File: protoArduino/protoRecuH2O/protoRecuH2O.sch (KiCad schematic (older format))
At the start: 1 part

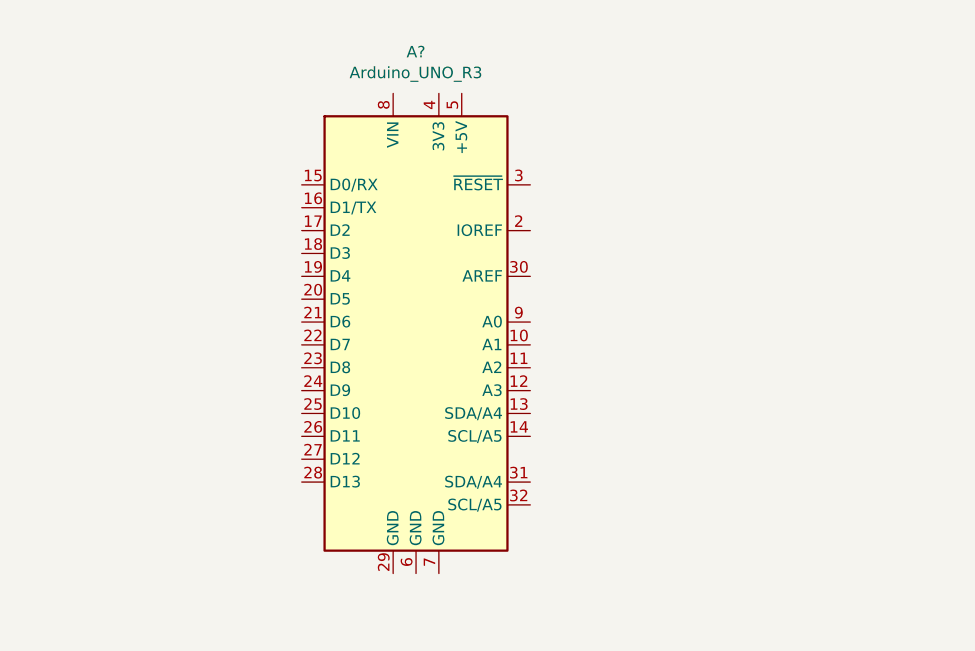
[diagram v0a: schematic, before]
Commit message: schéma éléctrique
j'ai ajouté la arduino, le graph bar, les résistances et le servo moteur avec tout le câblage. Il me reste plus que le câblage de la sonde à faire
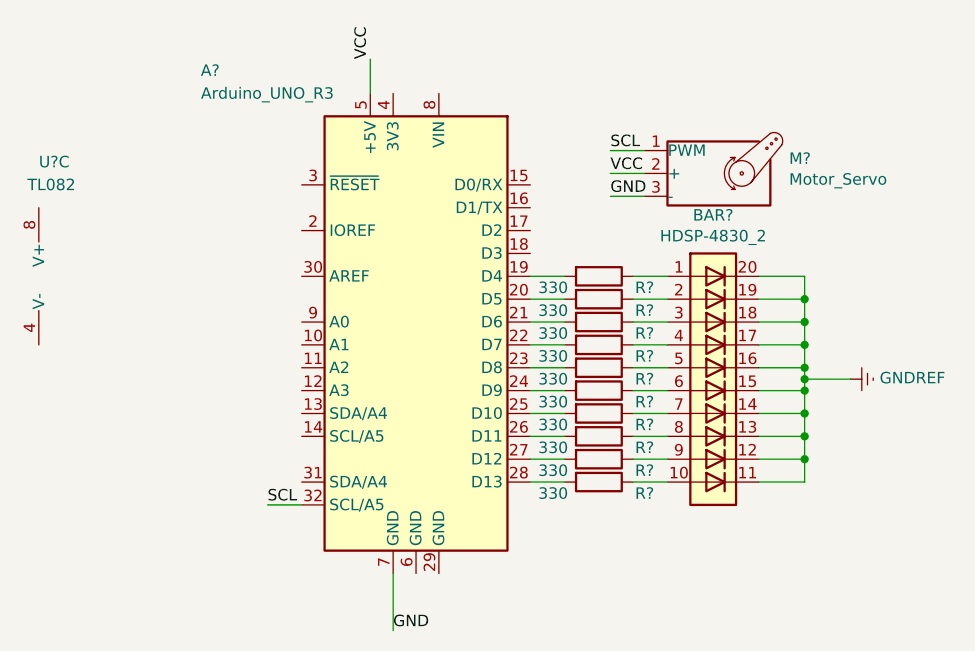
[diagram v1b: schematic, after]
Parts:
- added BAR?: HDSP-4830_2, Display:HDSP-4830, symbol LED:HDSP-4830_2
- added M?: Motor_Servo, symbol Motor:Motor_Servo
- added R? (x10): 330, symbol Device:R
- added U?: TL082, symbol Amplifier_Operational:TL082
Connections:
- net at A?.19 (D4): now also R?.2
- net at A?.20 (D5): now also R?.2
- net at A?.21 (D6): now also R?.2
- net at A?.22 (D7): now also R?.2
- net at A?.23 (D8): now also R?.2
- net at A?.24 (D9): now also R?.2
- net at A?.25 (D10): now also R?.2
- net at A?.26 (D11): now also R?.2
- net at A?.27 (D12): now also R?.2
- net at A?.28 (D13): now also R?.2
- net SCL: now reaches A?.32 (SCL/A5)
- net SCL: now also M?.1 (PWM)
- net VCC: now reaches A?.5 (+5V)
- net VCC: now also M?.2 (+)
- net GND: now reaches A?.7 (GND)
- net GND: now also M?.3 (-)
- new net: BAR?.1 (A), R?.1
- new net: BAR?.10 (A), R?.1
- new net: BAR?.2 (A), R?.1
- new net: BAR?.3 (A), R?.1
- new net: BAR?.4 (A), R?.1
- new net: BAR?.5 (A), R?.1
- new net: BAR?.6 (A), R?.1
- new net: BAR?.7 (A), R?.1
- new net: BAR?.8 (A), R?.1
- new net: BAR?.9 (A), R?.1
- new net GNDREF: BAR?.11 (K), BAR?.12 (K), BAR?.13 (K), BAR?.14 (K), BAR?.15 (K), BAR?.16 (K), BAR?.17 (K), BAR?.18 (K), BAR?.19 (K), BAR?.20 (K)
